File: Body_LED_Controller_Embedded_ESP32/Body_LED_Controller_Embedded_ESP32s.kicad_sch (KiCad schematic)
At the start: 101 parts, among them J1 SERIAL, J10 USB_B_Micro, J11 USB_B_Micro, J12 USB_B_Micro, J13 Conn_02x03_Odd_Even, J14 Conn_01x03, J15 Servo Header, J16 Screw_Terminal_01x02, J17 Screw_Terminal_01x02, J18 Screw_Terminal_01x02, J19 Screw_Terminal_01x02, J2 I2C, J20 ICSP, J3 Conn_02x10_Odd_Even, J4 LDP/MAINT, J5 COIN/VU, J6 Batt Level LEDS, J7 Data Panel/ CBI, J8 Spectrum Analyzer, J9 Ext Mic, SW1 SW_Push, SW2 SW_Push, SW3 SW_Push, U1 ATMEGA256016AU, U10 CH340C, U11 UMH3N, U12 ME6211C33M5G, U13 CJ2301_S1, U14 D36V50F5-STEPDOWN, U2 CH340C, U3 CJ2301_S1, U4 ESP32-WROOM-32U_16MB_, U5 CH340C, U6 UMH3N, U7 ME6211C33M5G, U8 CJ2301_S1, U9 ESP32-WROOM-32D_16MB_, Y1 16MHz

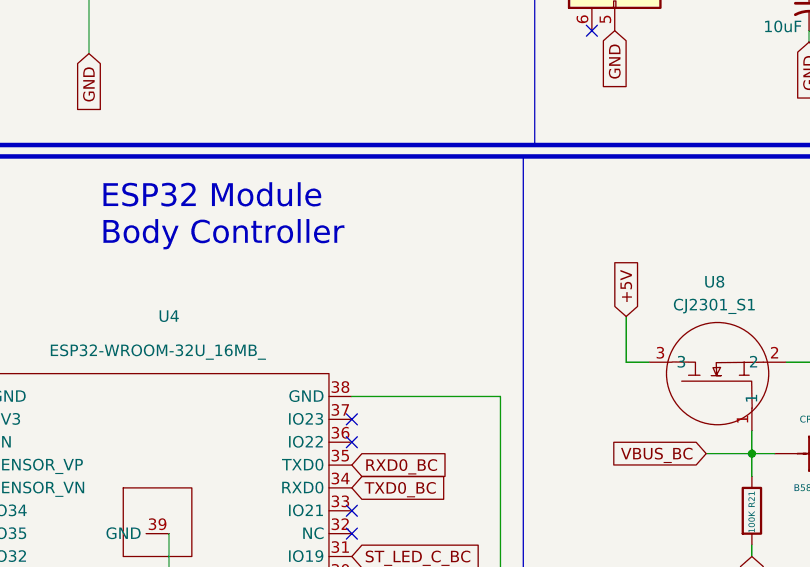
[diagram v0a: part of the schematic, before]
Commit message: Updated the body Controller to have SMA and u.fl interfaces for the 32U
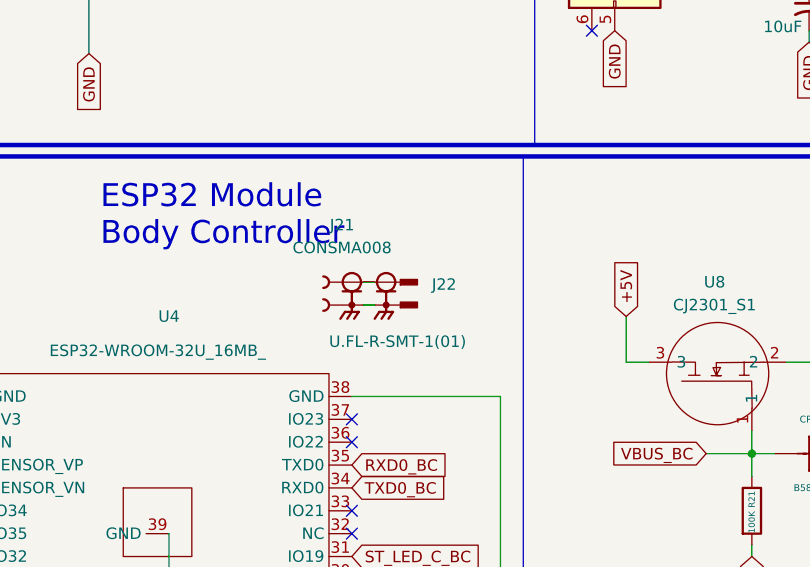
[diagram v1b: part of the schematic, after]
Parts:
- added J21: CONSMA008, Custom:LINX_CONSMA008, symbol Custom:CONSMA008
- added J22: U.FL-R-SMT-1(01), Custom:HIROSE_U.FL-R-SMT-1(01), symbol Custom:U.FL-R-SMT-1(01)
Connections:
- new net: J21.S1, J21.S2, J21.S3, J21.S4, J22.G1, J22.G2
- new net: J21.1, J22.SIG
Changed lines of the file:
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@@
     (stroke (width 0) (type default) (color 0 0 0 0))
   )
+  (wire (pts (xy 88.9 180.34) (xy 90.17 180.34))
+    (stroke (width 0) (type default) (color 0 0 0 0))
+  )
   (wire (pts (xy 68.58 113.03) (xy 54.61 113.03))
     (stroke (width 0) (type default) (color 0 0 0 0))
@@
     (stroke (width 0) (type default) (color 0 0 0 0))
   )
+  (wire (pts (xy 88.9 182.88) (xy 90.17 182.88))
+    (stroke (width 0) (type default) (color 0 0 0 0))
+  )
   (wire (pts (xy 379.73 128.27) (xy 379.73 115.57))
     (stroke (width 0) (type default) (color 0 0 0 0))
@@
     (pin "2")
   )
+  (symbol (lib_id "Custom:U.FL-R-SMT-1(01)") (at 91.44 180.34 0) (unit 1)
+    (in_bom yes) (on_board yes)
+    (property "Reference" "J22" (id 0) (at 96.52 180.5939 0)
+      (effects (font (size 1.27 1.27)) (justify left))
+    )
+    (property "Value" "U.FL-R-SMT-1(01)" (id 1) (at 85.09 186.9439 0)
+      (effects (font (size 1.27 1.27)) (justify left))
+    )
+    (property "Footprint" "Custom:HIROSE_U.FL-R-SMT-1(01)" (id 2) (at 91.44 180.34 0)
+      (effects (font (size 1.27 1.27)) (justify left bottom) hide)
+    )
+    (property "Datasheet" "" (id 3) (at 91.44 180.34 0)
+      (effects (font (size 1.27 1.27)) (justify left bottom) hide)
+    )
+    (property "PARTREV" "Jul.1.2022" (id 4) (at 91.44 180.34 0)
+      (effects (font (size 1.27 1.27)) (justify left bottom) hide)
+    )
+    (property "SNAPEDA_PN" "U.FL-R-SMT-1(01)" (id 5) (at 91.44 180.34 0)
+      (effects (font (size 1.27 1.27)) (justify left bottom) hide)
+    )
+    (property "MAXIMUM_PACKAGE_HEIGHT" "1.45mm" (id 6) (at 91.44 180.34 0)
+      (effects (font (size 1.27 1.27)) (justify left bottom) hide)
+    )
+    (property "STANDARD" "Manufacturer Recommendations" (id 7) (at 91.44 180.34 0)
+      (effects (font (size 1.27 1.27)) (justify left bottom) hide)
+    )
+    (property "MANUFACTURER" "Hirose" (id 8) (at 91.44 180.34 0)
+      (effects (font (size 1.27 1.27)) (justify left bottom) hide)
+    )
+    (pin "G1")
+    (pin "G2")
+    (pin "SIG")
+  )
   (symbol (lib_id "Device:C_Polarized_Small_US") (at 34.29 144.78 0) (unit 1)
     (in_bom yes) (on_board yes) (fields_autoplaced)
@@
     (pin "8")
   )
+  (symbol (lib_id "Custom:CONSMA008") (at 87.63 180.34 0) (unit 1)
+    (in_bom yes) (on_board yes) (fields_autoplaced)
+    (property "Reference" "J21" (id 0) (at 86.5505 173.99 0))
+    (property "Value" "CONSMA008" (id 1) (at 86.5505 176.53 0))
+    (property "Footprint" "Custom:LINX_CONSMA008" (id 2) (at 87.63 180.34 0)
+      (effects (font (size 1.27 1.27)) (justify left bottom) hide)
+    )
+    (property "Datasheet" "" (id 3) (at 87.63 180.34 0)
+      (effects (font (size 1.27 1.27)) (justify left bottom) hide)
+    )
+    (property "PARTREV" "A" (id 4) (at 87.63 180.34 0)
+      (effects (font (size 1.27 1.27)) (justify left bottom) hide)
+    )
+    (property "MAXIMUM_PACKAGE_HEIGHT" "13.88mm" (id 5) (at 87.63 180.34 0)
+      (effects (font (size 1.27 1.27)) (justify left bottom) hide)
+    )
+    (property "STANDARD" "Manufacturer Recommendations" (id 6) (at 87.63 180.34 0)
+      (effects (font (size 1.27 1.27)) (justify left bottom) hide)
+    )
+    (property "MANUFACTURER" "Linx Technologies" (id 7) (at 87.63 180.34 0)
+      (effects (font (size 1.27 1.27)) (justify left bottom) hide)
+    )
+    (pin "1")
+    (pin "S1")
+    (pin "S2")
+    (pin "S3")
+    (pin "S4")
+  )
   (symbol (lib_id "Device:C_Polarized_Small_US") (at 187.96 207.01 0) (unit 1)
     (in_bom yes) (on_board yes) (fields_autoplaced)
@@
       (reference "J20") (unit 1) (value "ICSP") (footprint "Connector_PinHeader_2.54mm:PinHeader_2x03_P2.54mm_Vertical")
     )
+    (path "/729d774e-6bf4-4f55-b472-f6716b55b263"
+      (reference "J21") (unit 1) (value "CONSMA008") (footprint "Custom:LINX_CONSMA008")
+    )
+    (path "/44998d1c-c3f3-4449-8388-86b040673494"
+      (reference "J22") (unit 1) (value "U.FL-R-SMT-1(01)") (footprint "Custom:HIROSE_U.FL-R-SMT-1(01)")
+    )
     (path "/e0a92b63-b80e-4806-aa72-1c7ed2738287"

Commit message: Updates to some files
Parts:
- removed D1, D2: LED, LED_SMD:LED_0402_1005Metric, symbol Device:LED
- removed D3, D4, D5: APA102-2020, LED_SMD:LED-APA102-2020, symbol LED:APA102-2020
- removed J21: CONSMA008, Custom:LINX_CONSMA008, symbol Custom:CONSMA008
- removed J22: U.FL-R-SMT-1(01), Custom:HIROSE_U.FL-R-SMT-1(01), symbol Custom:U.FL-R-SMT-1(01)
- removed RN1: 10K, Custom:SOIC127P762X240-14N, symbol Device:R_Network13
- added D1, D2: SMD-LED-CLEAR-BLUE(0402), Custom:LED-0402, symbol Custom:SMD-LED-CLEAR-BLUE(0402)
- added L1, L2, L3: WS2812B-2020, WS2812B-2020, symbol LED:WS2812B-2020
- added R29, R30, R31, R32, R33, R34, R35, R36, R37, R38: 10K, Resistor_SMD:R_0402_1005Metric, symbol Device:R
- C1, C2: LCSC (none) -> C1554
- C10, C11, C4, C5, C6, C7, C8, C9: LCSC (none) -> C307331
- C12, C15, C19, C22: symbol Device:C_Polarized_Small_US -> Device:C_Small; LCSC (none) -> C315248
- C13, C14, C16, C17, C18, C20, C21, C24, C25: symbol Device:C_Polarized_Small_US -> Device:C_Small; LCSC (none) -> C307331
- C23: symbol Device:C_Polarized_Small_US -> Device:C_Small
- C3: LCSC (none) -> C315248
- CR1: LCSC (none) -> C84354
- F1: LCSC (none) -> C17313
- J1, J2, J4: LCSC (none) -> C225519
- J10, J11, J12: LCSC (none) -> C132563
- J13, J20: LCSC (none) -> C390690
- J14, J9: LCSC (none) -> C390679
- J15, J8: LCSC (none) -> C190819
- J16, J17, J18, J19: LCSC (none) -> C474892
- J3: LCSC (none) -> C492427
- J5: LCSC (none) -> C225521
- J6: LCSC (none) -> C390680
- J7: LCSC (none) -> C390682
- R1: LCSC (none) -> C328343
- R10, R11, R12, R13, R14, R26, R6, R7, R8, R9: LCSC (none) -> C352454
- R15, R16, R2, R3: LCSC (none) -> C478866
- R17: LCSC (none) -> C269701
- R18: LCSC (none) -> C245983
- R19: LCSC (none) -> C325646
- R20, R23: LCSC (none) -> C190321
- R21, R22, R24, R25: LCSC (none) -> C365065
- R4, R5: LCSC (none) -> C269674
- SW1, SW2, SW3: LCSC (none) -> C692465
- U1: LCSC (none) -> C22460
- U10, U12, U2, U5, U7: LCSC (none) -> C82942
- U11, U6: LCSC (none) -> C62892
- U13, U3, U8: LCSC (none) -> C8547
- U4: LCSC (none) -> C529580
- U9: LCSC (none) -> C529578
- Y1: LCSC (none) -> C279575
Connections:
- net +3.3V_BC: now also L2.4 (VDD)
- net +3.3V_BS: now also L1.4 (VDD)
- net +5V_BL: now also L3.4 (VDD); no longer R15.1, R16.1
- net GND: now also R15.1, R16.1, L1.2 (VSS), L2.2 (VSS), L3.2 (VSS), R29.2, R30.2, R31.2, R32.2, R33.2, R34.2, R35.2, R36.2, R37.2, R38.2
- net LIMIT1: now also R29.1
- net LIMIT10: now also R38.1
- net LIMIT2: now also R30.1
- net LIMIT3: now also R31.1
- net LIMIT4: now also R32.1
- net LIMIT5: now also R33.1
- net LIMIT6: now also R34.1
- net LIMIT7: now also R35.1
- net LIMIT8: now also R36.1
- net LIMIT9: now also R37.1
- net RXD0_BL: now also D2.+
- net TXD0_BL: now also D1.+
- net at R28.1: now also L1.3 (DI)
- net at R26.1: now also L3.3 (DI)
- net at R15.2: now also D1.-
- net at R27.1: now also L2.3 (DI)
- net at R16.2: now also D2.-
- net ST_LED_C_BC: no longer names the net of U4.31 (IO19)
- net ST_LED_C_BL: no longer names the net of U1.16 (PH4)
- net ST_LED_C_BS: no longer names the net of U9.31 (IO19)
- no-connect marks 123 -> 122
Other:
- moved on the sheet: R26, R27, R28

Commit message: updates to the boards
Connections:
- net RXD0_BC: no longer U4.35 (TXD0)
- net RXD0_BL: now also U1.2 (PE0); no longer U1.3 (PE1)
- net RXD0_BS: now also U9.34 (RXD0); no longer U9.35 (TXD0)
- net TXD0_BC: now also U4.35 (TXD0); no longer U4.34 (RXD0)
- net TXD0_BL: now also U1.3 (PE1); no longer U1.2 (PE0)
- net TXD0_BS: now also U9.35 (TXD0); no longer U9.34 (RXD0)
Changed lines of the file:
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@@
     )
   )
-  (global_label "TXD0_BS" (shape input) (at 88.9 104.14 0) (fields_autoplaced)
-    (effects (font (size 1.27 1.27)) (justify left))
-    (property "Intersheet References" "${INTERSHEET_REFS}" (id 0) (at 99.328 104.2194 0)
+  (global_label "TXD0_BS" (shape input) (at 88.9 101.6 0) (fields_autoplaced)
+    (effects (font (size 1.27 1.27)) (justify left))
+    (property "Intersheet References" "${INTERSHEET_REFS}" (id 0) (at 99.328 101.6794 0)
       (effects (font (size 1.27 1.27)) (justify left) hide)
     )
@@
     )
   )
-  (global_label "RXD0_BS" (shape input) (at 88.9 101.6 0) (fields_autoplaced)
-    (effects (font (size 1.27 1.27)) (justify left))
-    (property "Intersheet References" "${INTERSHEET_REFS}" (id 0) (at 99.6304 101.6794 0)
-      (effects (font (size 1.27 1.27)) (justify left) hide)
-    )
-  )
-  (global_label "RXD0_BC" (shape input) (at 87.63 200.66 0) (fields_autoplaced)
-    (effects (font (size 1.27 1.27)) (justify left))
-    (property "Intersheet References" "${INTERSHEET_REFS}" (id 0) (at 98.4209 200.7394 0)
+  (global_label "RXD0_BS" (shape input) (at 88.9 104.14 0) (fields_autoplaced)
+    (effects (font (size 1.27 1.27)) (justify left))
+    (property "Intersheet References" "${INTERSHEET_REFS}" (id 0) (at 99.6304 104.2194 0)
+      (effects (font (size 1.27 1.27)) (justify left) hide)
+    )
+  )
+  (global_label "RXD0_BC" (shape input) (at 88.9 203.2 0) (fields_autoplaced)
+    (effects (font (size 1.27 1.27)) (justify left))
+    (property "Intersheet References" "${INTERSHEET_REFS}" (id 0) (at 99.6909 203.2794 0)
       (effects (font (size 1.27 1.27)) (justify left) hide)
     )
@@
     )
   )
-  (global_label "RXD0_BL" (shape input) (at 321.31 146.05 180) (fields_autoplaced)
-    (effects (font (size 1.27 1.27)) (justify right))
-    (property "Intersheet References" "${INTERSHEET_REFS}" (id 0) (at 310.761 145.9706 0)
+  (global_label "RXD0_BL" (shape input) (at 321.31 143.51 180) (fields_autoplaced)
+    (effects (font (size 1.27 1.27)) (justify right))
+    (property "Intersheet References" "${INTERSHEET_REFS}" (id 0) (at 310.761 143.4306 0)
       (effects (font (size 1.27 1.27)) (justify right) hide)
     )
@@
     )
   )
-  (global_label "TXD0_BC" (shape input) (at 87.63 203.2 0) (fields_autoplaced)
-    (effects (font (size 1.27 1.27)) (justify left))
-    (property "Intersheet References" "${INTERSHEET_REFS}" (id 0) (at 98.1185 203.2794 0)
+  (global_label "TXD0_BC" (shape input) (at 87.63 200.66 0) (fields_autoplaced)
+    (effects (font (size 1.27 1.27)) (justify left))
+    (property "Intersheet References" "${INTERSHEET_REFS}" (id 0) (at 98.1185 200.7394 0)
       (effects (font (size 1.27 1.27)) (justify left) hide)
     )
@@
     )
   )
-  (global_label "TXD0_BL" (shape input) (at 321.31 143.51 180) (fields_autoplaced)
-    (effects (font (size 1.27 1.27)) (justify right))
-    (property "Intersheet References" "${INTERSHEET_REFS}" (id 0) (at 311.0634 143.4306 0)
-      (effects (font (size 1.27 1.27)) (justify right) hide)
-    )
+  (global_label "TXD0_BL" (shape input) (at 321.31 146.05 180) (fields_autoplaced)
+    (effects (font (size 1.27 1.27)) (justify right))
+    (property "Intersheet References" "${INTERSHEET_REFS}" (id 0) (at 311.0634 145.9706 0)
+      (effects (font (size 1.27 1.27)) (justify right) hide)
+    )
